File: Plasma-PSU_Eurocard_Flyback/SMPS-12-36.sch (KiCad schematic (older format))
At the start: 43 parts

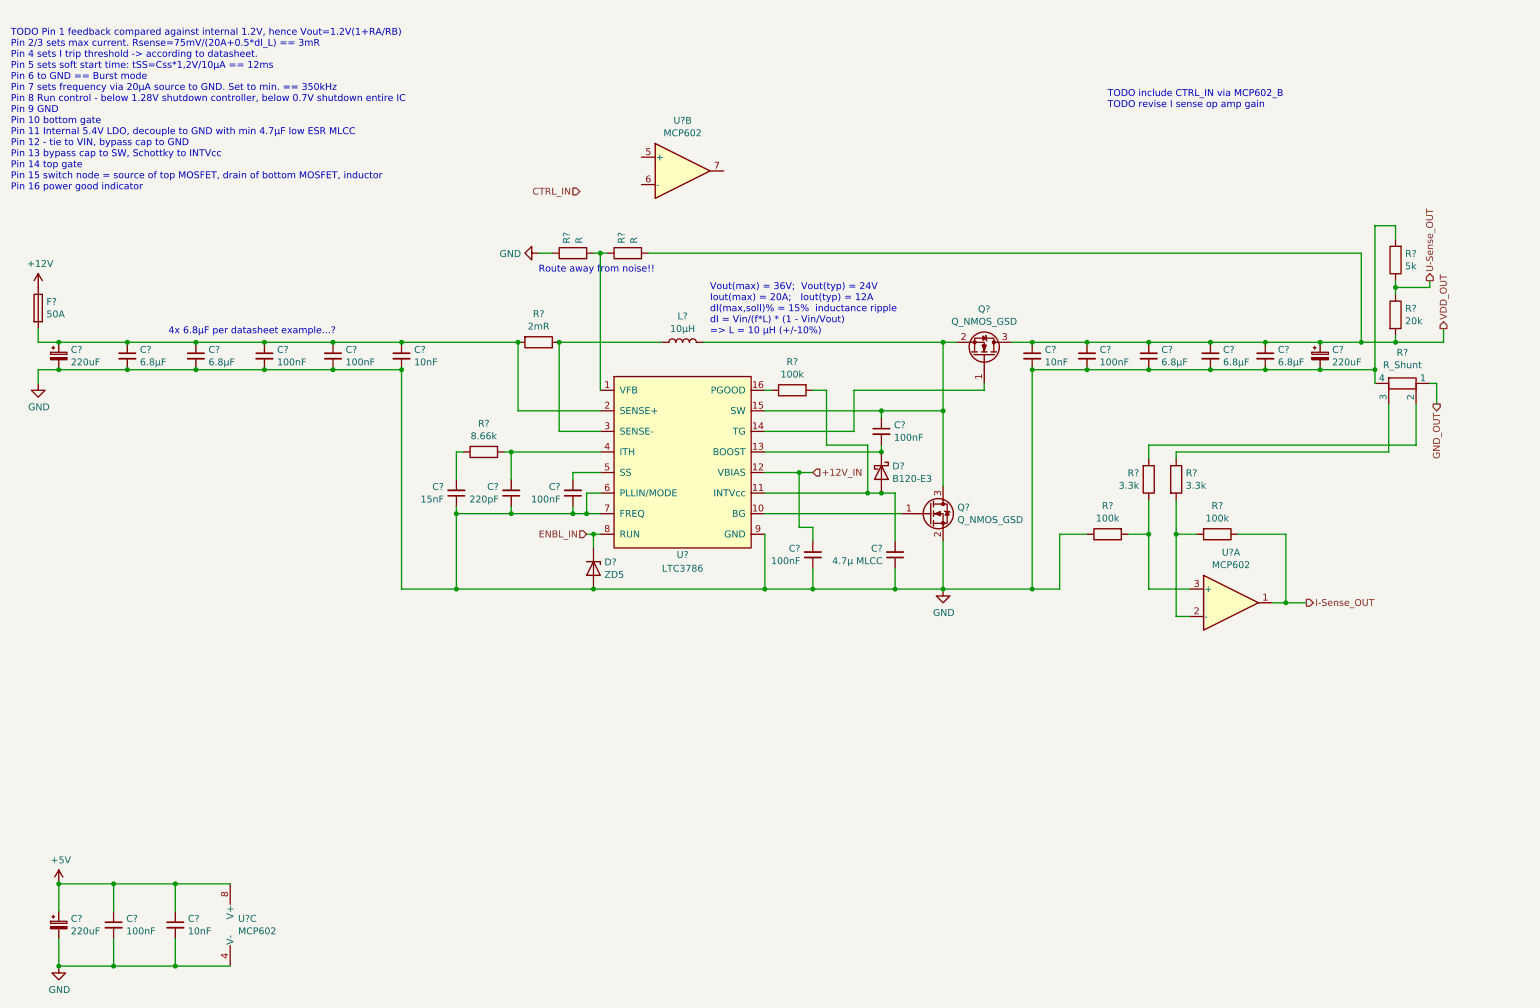
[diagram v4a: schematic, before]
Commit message: Filters for sense signals
- RC filters on U-sense and I-sense included
- Block diagram refined
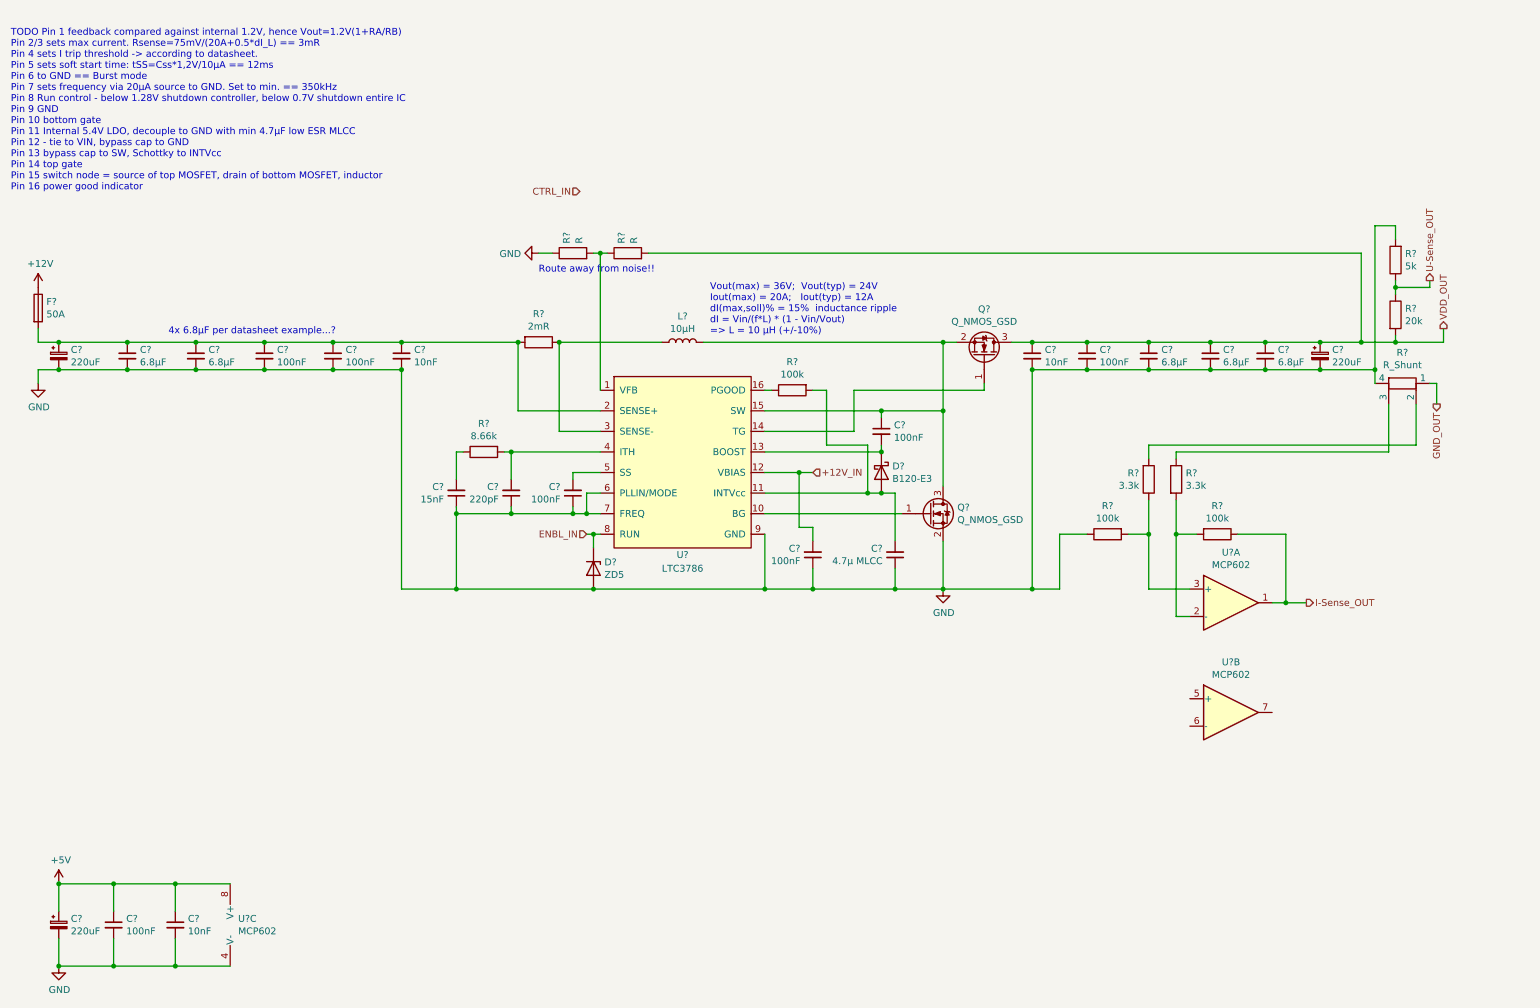
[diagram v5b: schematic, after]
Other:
- note removed: "TODO include CTRL_IN via MCP602_B\nTODO revise I sense op amp gain"
- moved on the sheet: U?B
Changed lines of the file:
@@
 Sheet 5 5
 Title "Plasma-PSU_Eurocard_Flyback"
-Date "2020-04-07"
-Rev "0.0.3"
+Date "2020-04-08"
+Rev "0.0.4"
 Comp "University of Ljubljana"
 Comment1 "Biotechnical faculty"
@@
 L Amplifier_Operational:MCP602 U?
 U 2 1 5E8D15DA
-P 5550 1700
-F 0 "U?" H 5550 2067 50  0000 C CNN
-F 1 "MCP602" H 5550 1976 50  0000 C CNN
-F 2 "" H 5550 1700 50  0001 C CNN
-F 3 "http://ww1.microchip.com/downloads/en/DeviceDoc/21314g.pdf" H 5550 1700 50  0001 C CNN
-	2    5550 1700
+P 9550 5650
+F 0 "U?" H 9550 6017 50  0000 C CNN
+F 1 "MCP602" H 9550 5926 50  0000 C CNN
+F 2 "" H 9550 5650 50  0001 C CNN
+F 3 "http://ww1.microchip.com/downloads/en/DeviceDoc/21314g.pdf" H 9550 5650 50  0001 C CNN
+	2    9550 5650
 	1    0    0    -1
 $EndComp
@@
 	6150 4750 4900 4750
 Connection ~ 6150 4750
-Text Notes 8650 1250 0    50   ~ 0
-TODO include CTRL_IN via MCP602_B\nTODO revise I sense op amp gain
 $Comp
 L Device:D_Zener D?

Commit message: DAC sets U_out
DAC converter in SMPS sheet sets boost modules output voltage.
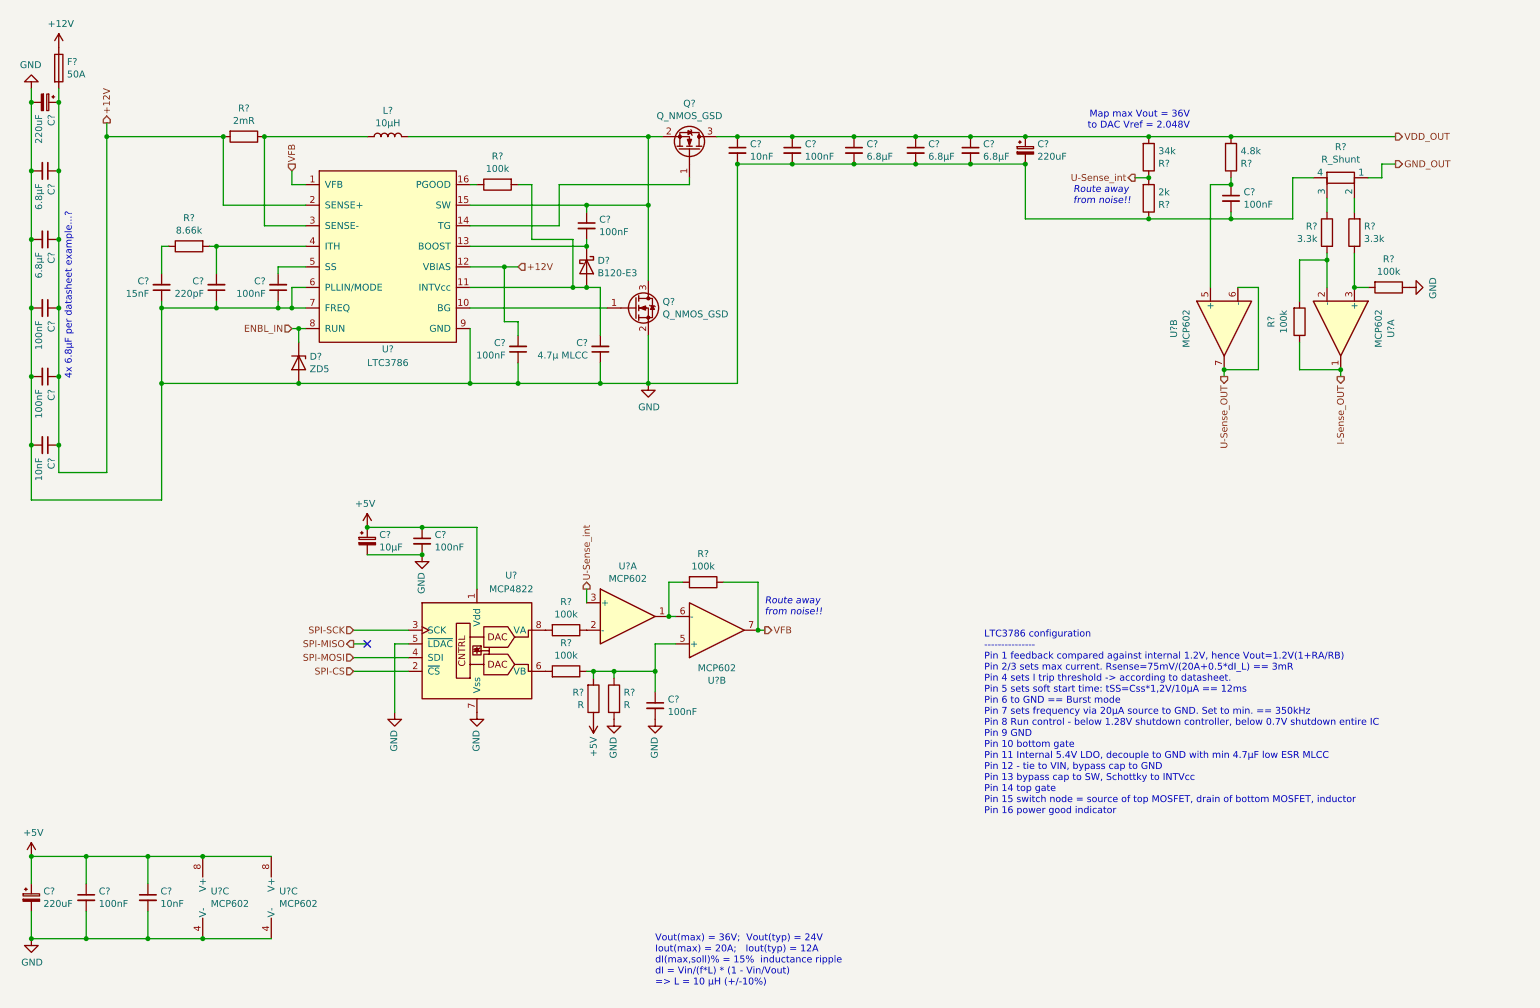
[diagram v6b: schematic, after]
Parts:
- removed R?: 5k, symbol Device:R
- removed R? (x2): R, symbol Device:R
- added C?: 10µF, symbol Device:CP_Small
- added C? (x3): 100nF, symbol Device:C_Small
- added R? (x3): 100k, symbol Device:R
- added R? (x2): R, symbol Device:R
- added R?: 34k, symbol Device:R
- added R?: 2k, symbol Device:R
- added U?: MCP4822, symbol Analog_DAC:MCP4822
- added U? (x3): MCP602, symbol Amplifier_Operational:MCP602
- R?: value 20k -> 4.8k
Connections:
- net +12V_IN is gone; now on net +12V: C?.2, U?.12 (VBIAS)
- net +12V: now also C?.1, C?.1, C?.1, C?.1, C?.1, C?.1, F?.2, R?.2, U?.2 (SENSE+)
- net +5V: now also C?.1, C?.1, R?.1, U?.1 (Vdd), U?.8 (V+)
- net GND: now also C?.2, C?.2, C?.2, C?.2, R?.1, R?.2, U?.4 (V-), U?.5 (~LDAC), U?.7 (Vss)
- net U-Sense_OUT: now also U?.6 (-), U?.7; no longer R?.1
- net VDD_OUT: now also R?.2
- net at U?.5 (+): now also C?.1, R?.1, R?.1, R?.2
- net at U?.6 (-): now also R?.2, U?.1
- net VFB: now reaches U?.7
- net VFB: now also U?.1 (VFB), R?.1
- new net: C?.1, R?.1, U?.5 (+)
- new net: R?.2, U?.6 (VB)
- new net: R?.2, U?.8 (VA)
- new net: R?.1, U?.2 (-)
- new net SPI-CS: U?.2 (~CS)
- new net SPI-MOSI: U?.4 (SDI)
- new net SPI-SCK: U?.3 (SCK)
- new net U-Sense_int: R?.1, R?.2, U?.3 (+)
- no-connect marks 0 -> 1
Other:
- note added: "LTC3786 configuration\n---------------\nPin 1 feedback compared against internal 1.2V, hence Vout=1.2V(1+RA/RB)\nPin 2/3 sets max current. Rsense=75mV/(20A+0.5*dI_L) == 3mR \nPin 4 sets I trip threshold -> according to datasheet.\nPin 5 sets soft start time: tSS=Css*1,2V/10µA == 12ms\nPin 6 to GND == Burst mode\nPin 7 sets frequency via 20µA source to GND. Set to min. == 350kHz\nPin 8 Run control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"
- note added: "Map max Vout = 36V \nto DAC Vref = 2.048V"
- note added: "Route away \nfrom noise!!"
- note removed: "Route away from noise!!"
- note removed: "TODO Pin 1 feedback compared against internal 1.2V, hence Vout=1.2V(1+RA/RB)\nPin 2/3 sets max current. Rsense=75mV/(20A+0.5*dI_L) == 3mR \nPin 4 sets I trip threshold -> according to datasheet.\nPin 5 sets soft start time: tSS=Css*1,2V/10µA == 12ms\nPin 6 to GND == Burst mode\nPin 7 sets frequency via 20µA source to GND. Set to min. == 350kHz\nPin 8 Run control - below 1.28V shutdown controller,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"
- moved on the sheet: C?, D?, F?, L?, Q?, R?, U?, U?A, U?B, U?C

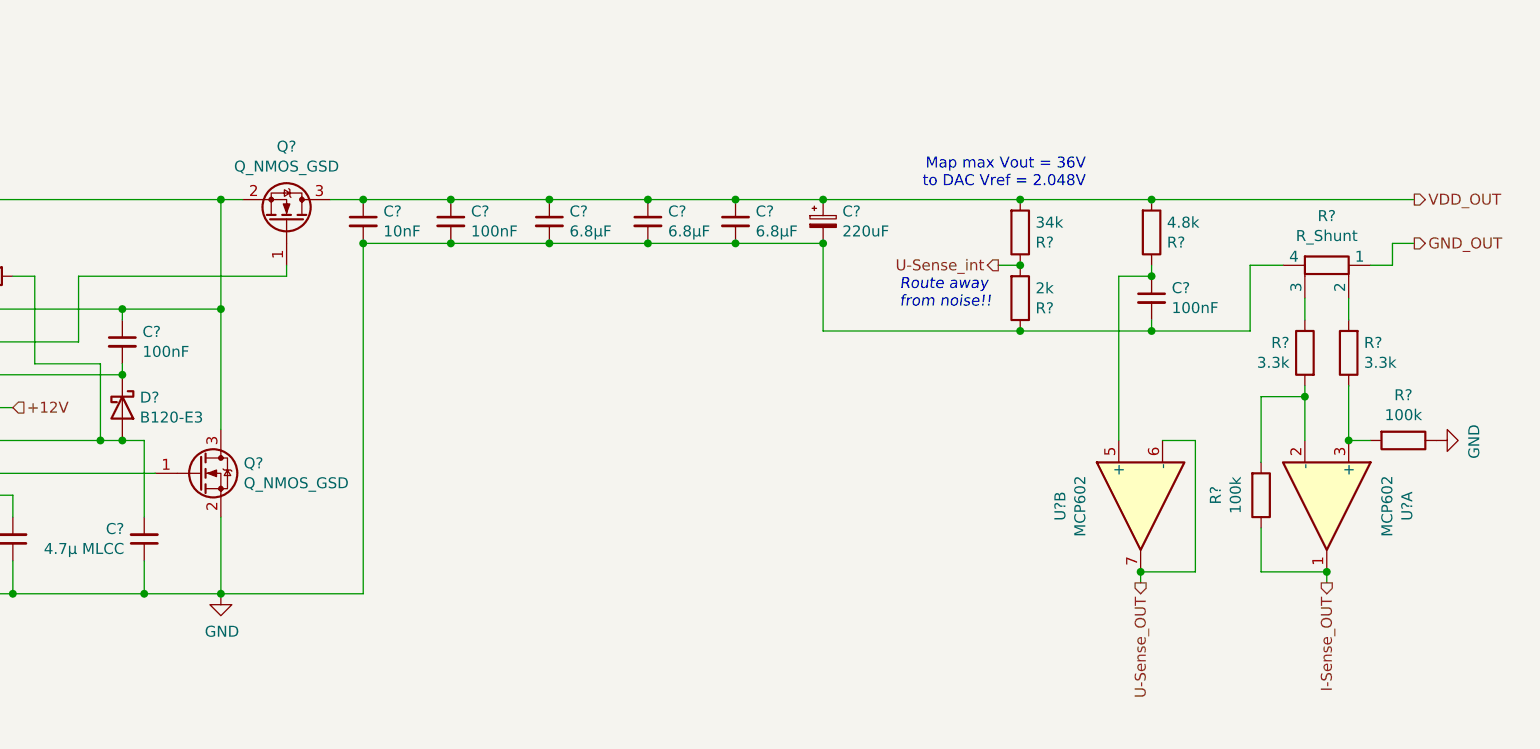
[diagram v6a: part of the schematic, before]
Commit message: SMPS & Shunt selected
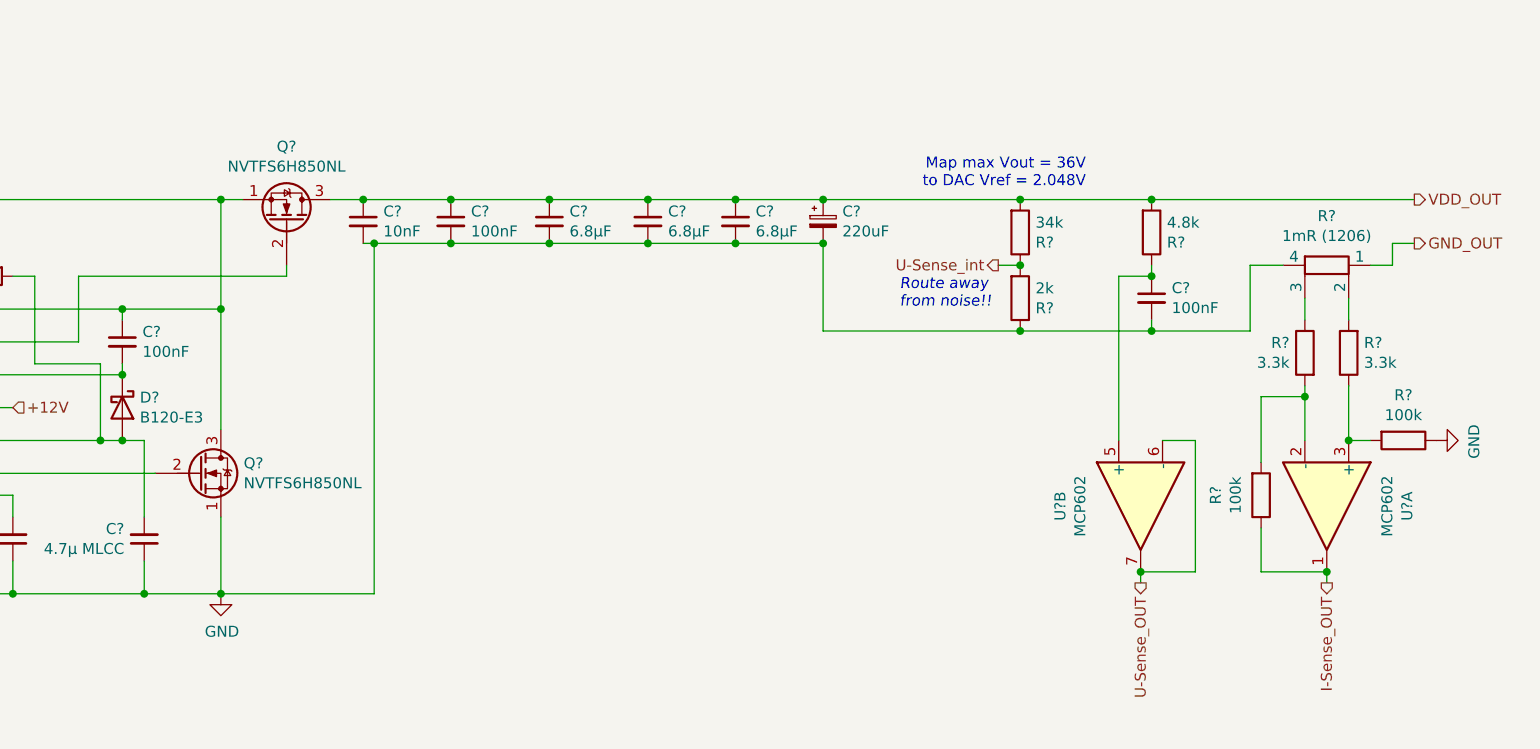
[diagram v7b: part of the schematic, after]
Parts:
- removed Q? (x2): Q_NMOS_GSD, symbol Device:Q_NMOS_GSD
- added Q? (x2): NVTFS6H850NL, symbol Device:Q_NMOS_SGD
- R?: value R_Shunt -> 1mR (1206)
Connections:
- net GND: now also Q?.1 (S)
- net VDD_OUT: now also Q?.3 (D)
- net at U?.10 (BG): now also Q?.2 (G)
- net at U?.14 (TG): now also Q?.2 (G)
- net at C?.1, L?.2, U?.15 (SW): now also Q?.1 (S), Q?.3 (D)
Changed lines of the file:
@@
-$EndComp
-$Comp
-L Device:Q_NMOS_GSD Q?
-U 1 1 5E952E7F
-P 5600 1550
-F 0 "Q?" V 5942 1550 50  0000 C CNN
-F 1 "Q_NMOS_GSD" V 5851 1550 50  0000 C CNN
-F 2 "" H 5800 1650 50  0001 C CNN
-F 3 "~" H 5600 1550 50  0001 C CNN
-	1    5600 1550
-	0    1    -1   0
-$EndComp
-$Comp
-L Device:Q_NMOS_GSD Q?
-U 1 1 5E953579
-P 5200 2700
-F 0 "Q?" H 5404 2746 50  0000 L CNN
-F 1 "Q_NMOS_GSD" H 5404 2655 50  0000 L CNN
-F 2 "" H 5400 2800 50  0001 C CNN
-F 3 "~" H 5200 2700 50  0001 C CNN
-	1    5200 2700
-	1    0    0    -1
 $EndComp
 $Comp
@@
 	4650 1800 5600 1800
 Wire Wire Line
-	5950 3250 5950 1650
+	6000 3250 6000 1650
 Wire Wire Line
 	800  1200 800  1100
@@
 	1    0    0    -1
 $EndComp
-Connection ~ 5950 1650
-Wire Wire Line
-	5300 3250 5950 3250
 Text Notes 5350 7650 0    50   ~ 0
 Vout(max) = 36V;  Vout(typ) = 24V\nIout(max) = 20A;   Iout(typ) = 12A\ndI(max,soll)% = 15%  inductance ripple\ndI = Vin/(f*L) * (1 - Vin/Vout)\n=> L = 10 µH (+/-10%)
@@
 	7250 1650 7650 1650
 Wire Wire Line
-	5950 1650 6350 1650
+	5950 1650 6000 1650
 Wire Wire Line
 	5950 1450 6350 1450
@@
 P 10350 1750
 F 0 "R?" V 10125 1750 50  0000 C CNN
-F 1 "R_Shunt" V 10216 1750 50  0000 C CNN
+F 1 "1mR (1206)" V 10216 1750 50  0000 C CNN
 F 2 "" V 10280 1750 50  0001 C CNN
 F 3 "~" H 10350 1750 50  0001 C CNN
@@
 Text Notes 6150 4950 0    50   Italic 0
 Route away \nfrom noise!!
+$Comp
+L Device:Q_NMOS_SGD Q?
+U 1 1 5E9117BD
+P 5200 2700
+F 0 "Q?" H 5404 2746 50  0000 L CNN
+F 1 "NVTFS6H850NL" H 5404 2655 50  0000 L CNN
+F 2 "" H 5400 2800 50  0001 C CNN
+F 3 "~" H 5200 2700 50  0001 C CNN
+	1    5200 2700
+	1    0    0    -1
+$EndComp
+Connection ~ 6000 1650
+Wire Wire Line
+	6000 1650 6350 1650
+Wire Wire Line
+	5300 3250 6000 3250
+$Comp
+L Device:Q_NMOS_SGD Q?
+U 1 1 5E92209C
+P 5600 1550
+F 0 "Q?" V 5942 1550 50  0000 C CNN
+F 1 "NVTFS6H850NL" V 5851 1550 50  0000 C CNN
+F 2 "" H 5800 1650 50  0001 C CNN
+F 3 "~" H 5600 1550 50  0001 C CNN
+	1    5600 1550
+	0    1    -1   0
+$EndComp
 $EndSCHEMATC
